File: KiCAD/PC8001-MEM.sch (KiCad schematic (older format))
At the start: 29 parts, among them J1 PC-8001 ext BUS, U1 74LS32, U10 ULN2803A, U2 74LS138, U3 74LS32, U4 74LS74, U5 74LS138, U6 74LS541, U7 74LS273, U8 74LS541, U9 628128

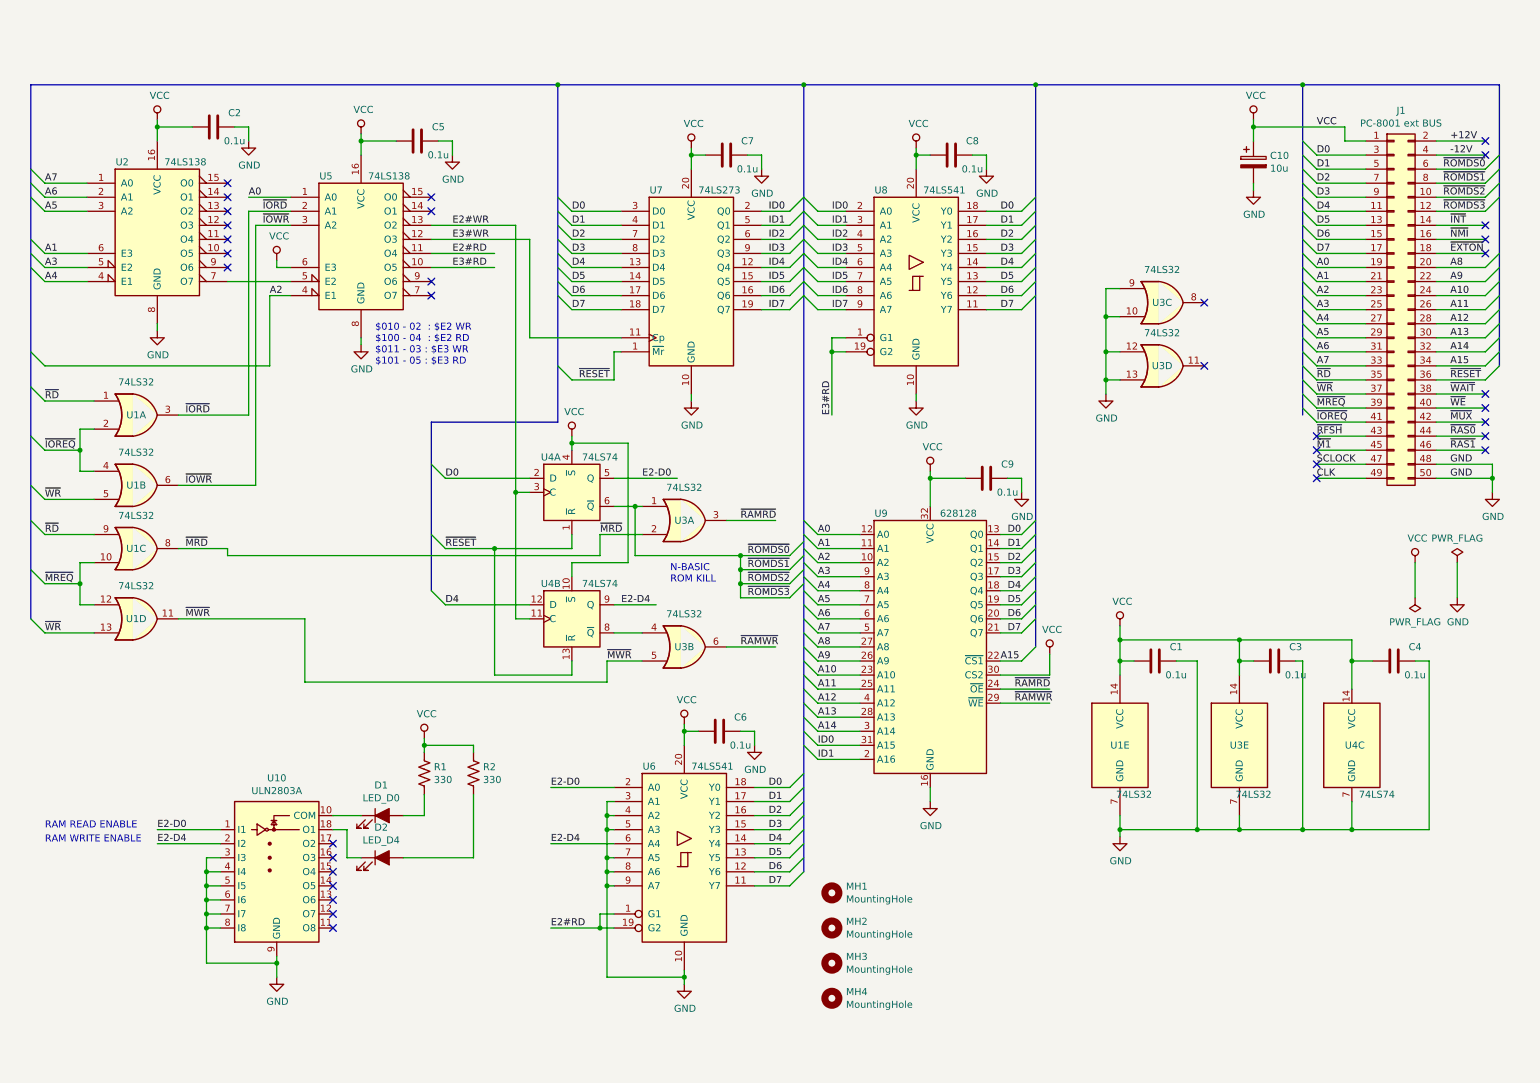
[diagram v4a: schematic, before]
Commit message: E2hのレジスタを74LS175へ変更、LEDドライバ変更
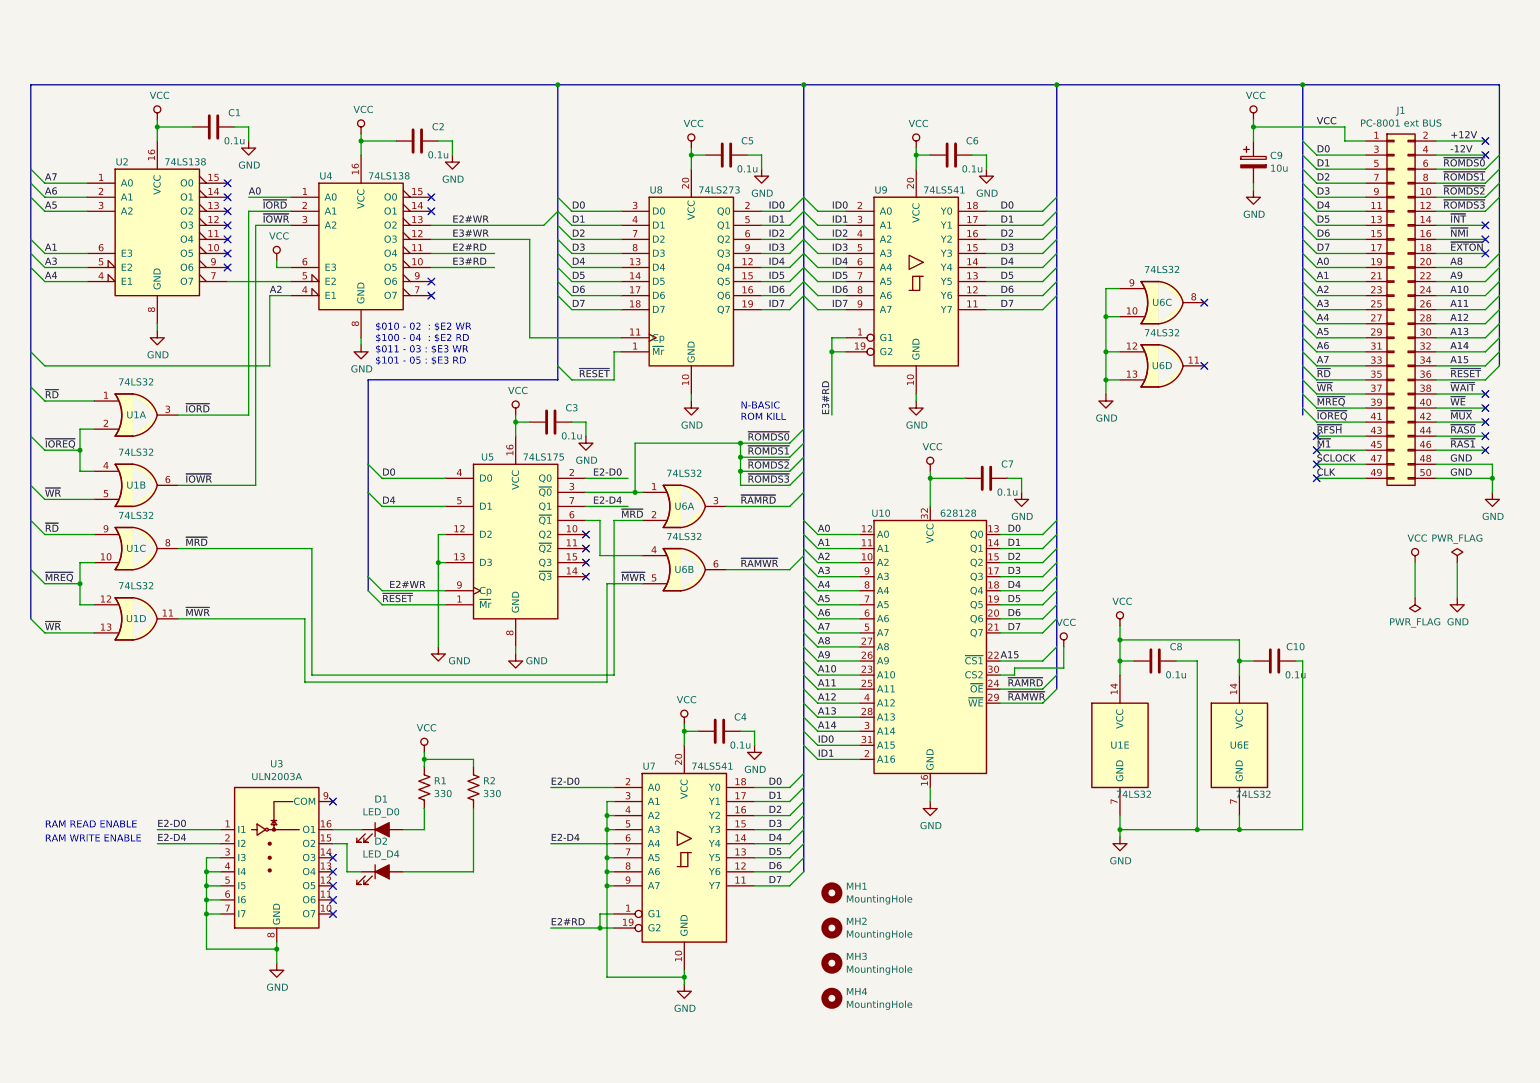
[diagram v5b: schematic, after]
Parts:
- removed C4: 0.1u, Capacitor_THT:C_Disc_D3.0mm_W1.6mm_P2.50mm, symbol Device:C
- removed U10: ULN2803A, symbol Transistor_Array:ULN2803A
- removed U4: 74LS74, symbol 74xx:74LS74
- added C3: 0.1u, Capacitor_THT:C_Disc_D3.0mm_W1.6mm_P2.50mm, symbol Device:C
- added U3: ULN2003A, symbol Transistor_Array:ULN2003A
- added U5: 74LS175, symbol 74xx:74LS175
- renumbered C2 to C1, C3 to C10, C5 to C2, C6 to C4, C7 to C5, C8 to C6, C9 to C7, C1 to C8, C10 to C9, U9 to U10, U5 to U4, U3 to U6, U6 to U7, U7 to U8, U8 to U9
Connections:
- net D0: now also U5.4 (D0)
- net D4: now also U5.5 (D1)
- net E2#WR: now also U5.9 (Cp)
- net E2-D0: now also U3.1 (I1), U5.2 (Q0)
- net E2-D4: now also U3.2 (I2), U5.7 (Q1)
- net GND: now also C3.1, U3.3 (I3), U3.4 (I4), U3.5 (I5), U3.6 (I6), U3.7 (I7), U3.8 (GND), U5.12 (D2), U5.13 (D3), U5.8 (GND)
- net VCC: now also C3.2, U5.16 (VCC)
- net ~RESET: now also U5.1 (~Mr)
- net ~ROMDS0: now also U5.3 (~Q0)
- net at U6.4: now also U5.6 (~Q1)
- net at D1.1 (K): now also U3.16 (O1)
- net at D2.1 (K): now also U3.15 (O2)
- no-connect marks 34 -> 37
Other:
- moved on the sheet: D1, D2, R1, R2, U6A, U6B

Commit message: プリント基板化検討
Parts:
- added D2: LED_ID0, LED_THT:LED_D3.0mm, symbol Device:LED_ALT
- added D3: LED_ID1, LED_THT:LED_D3.0mm, symbol Device:LED_ALT
- added R3, R4: 1k, Resistor_THT:R_Axial_DIN0207_L6.3mm_D2.5mm_P10.16mm_Horizontal, symbol Device:R_US
- C9: footprint (none) -> Capacitor_THT:CP_Radial_D5.0mm_P2.50mm
- D1: footprint (none) -> LED_THT:LED_D3.0mm
- D4: renamed from D2; footprint (none) -> LED_THT:LED_D3.0mm
- J1: footprint (none) -> Connector_PinHeader_2.54mm:PinHeader_2x25_P2.54mm_Horizontal
- R1, R2: value 330 -> 1k; footprint (none) -> Resistor_THT:R_Axial_DIN0207_L6.3mm_D2.5mm_P10.16mm_Horizontal
- U1, U6: footprint (none) -> Package_DIP:DIP-14_W7.62mm_Socket
- U10: footprint (none) -> Package_DIP:DIP-32_W15.24mm_Socket
- U2, U3, U4, U5: footprint (none) -> Package_DIP:DIP-16_W7.62mm_Socket
- U7, U8, U9: footprint (none) -> Package_DIP:DIP-20_W7.62mm_Socket
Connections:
- net GND: no longer U3.3 (I3), U3.4 (I4)
- net ID0: now also U3.3 (I3)
- net ID1: now also U3.4 (I4)
- net VCC: now also R3.1, R4.1
- net at U3.13 (O4): now also D3.1 (K)
- net at U3.14 (O3): now also D2.1 (K)
- new net: D2.2 (A), R3.2
- new net: D3.2 (A), R4.2
- no-connect marks 37 -> 35
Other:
- note added: "BANK_NO"
- moved on the sheet: D1, D4, R1, R2, U3

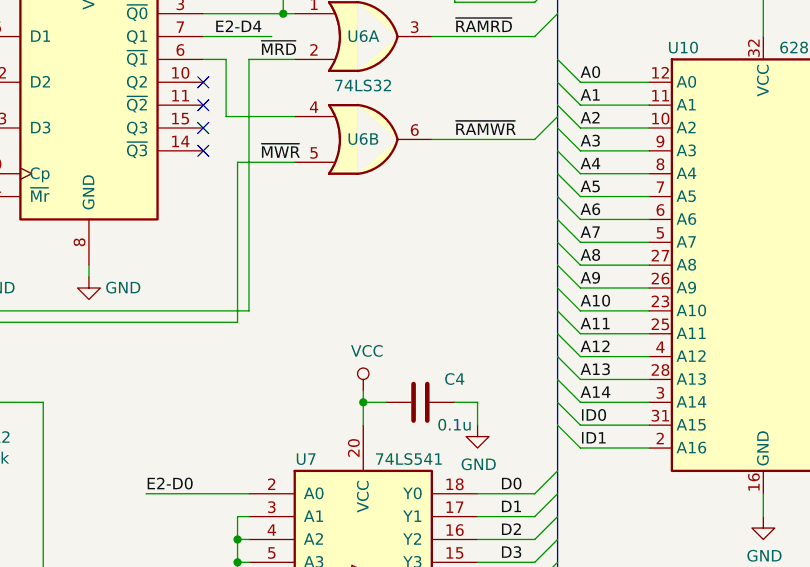
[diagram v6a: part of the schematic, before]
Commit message: 8k SRAMボードコントロール信号端子追加・ガーバーデータ再出力
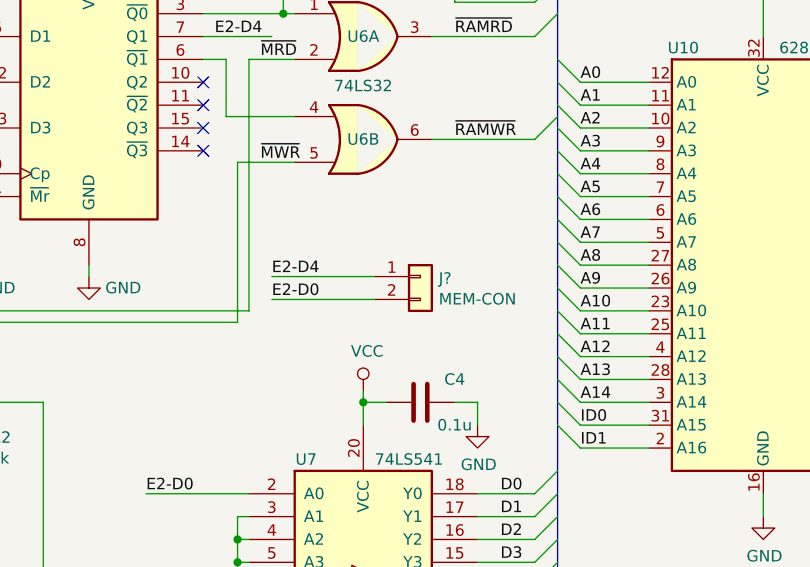
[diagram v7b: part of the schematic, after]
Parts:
- added J?: MEM-CON, symbol Connector_Generic:Conn_01x02
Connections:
- net E2-D0: now also J?.2 (Pin_2)
- net E2-D4: now also J?.1 (Pin_1)
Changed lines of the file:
@@
 Wire Wire Line
 	1750 6600 1650 6600
+Connection ~ 1650 6600
+Wire Wire Line
+	1650 6600 1650 6700
+$Comp
+L Connector_Generic:Conn_01x02 J?
+U 1 1 604F91E9
+P 5500 5050
+F 0 "J?" H 5580 5042 50  0000 L CNN
+F 1 "MEM-CON" H 5580 4951 50  0000 L CNN
+F 2 "" H 5500 5050 50  0001 C CNN
+F 3 "~" H 5500 5050 50  0001 C CNN
+	1    5500 5050
+	1    0    0    -1
+$EndComp
+Wire Wire Line
+	4850 5150 5300 5150
+Text Label 4850 5150 0    50   ~ 0
+E2-D0
+Wire Wire Line
+	4850 5050 5300 5050
+Text Label 4850 5050 0    50   ~ 0
+E2-D4
 Wire Bus Line
 	3000 3100 3000 4600
@@
 Wire Bus Line
 	6100 1000 6100 6600
-Connection ~ 1650 6600
-Wire Wire Line
-	1650 6600 1650 6700
 $EndSCHEMATC
